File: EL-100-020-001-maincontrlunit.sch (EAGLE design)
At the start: 186 parts, among them T1 WS-TST-90°, U1 VNI4140K-32, U16 24AA256-I/SN, U19 ABS10-32.768KHZ-7-T, U2 VNI4140K-32, U3 VNI4140K-32, U8 MCP7940N-I/SN, U9 PMEG2005ET, X1 944-12-46-00, X10 S2L3.50/8/90G, X11 S2L3.50/8/90G, X12 S2L3.50/8/90G, X13 140-08-FLACHBAND1.27, X14 944-12-2-00, X2 944-12-46-00, X3 90G-14, X4 90G-14, X5 Q-063209, X6 Q-063209, X7 Q-063209, X8 Q-063209, X9 S2L3.50/8/90G

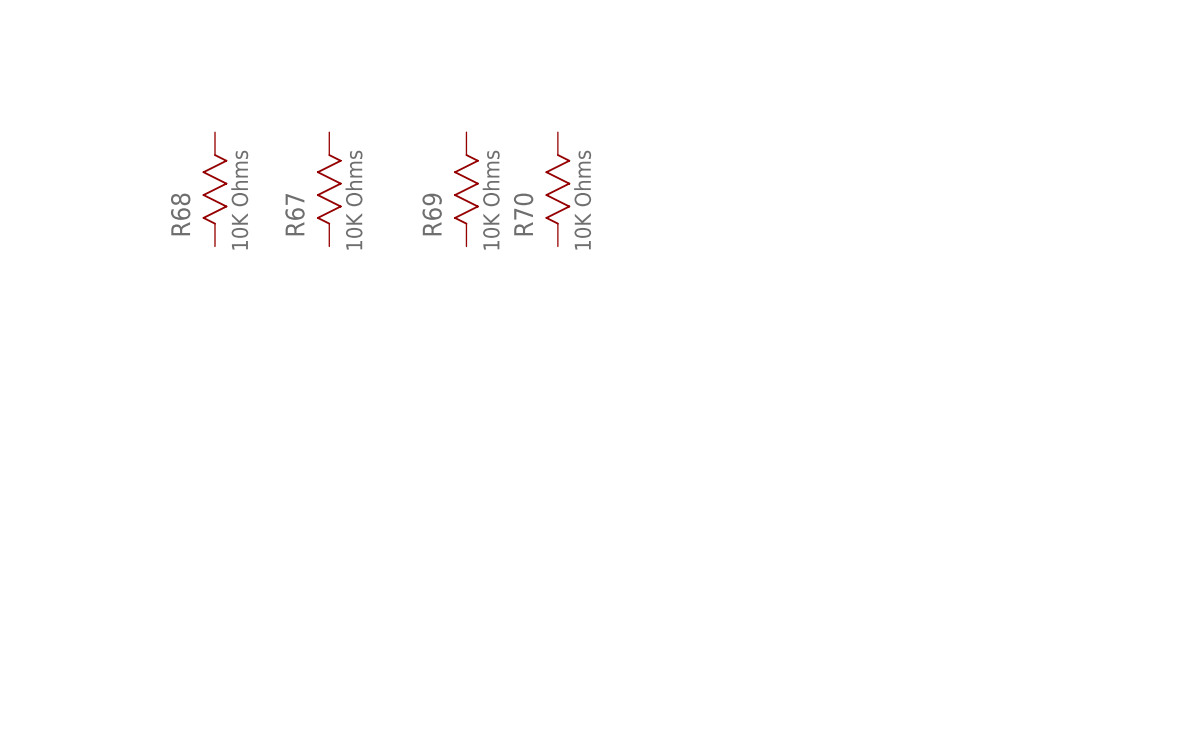
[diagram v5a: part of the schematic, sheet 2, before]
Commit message: update DIN rail
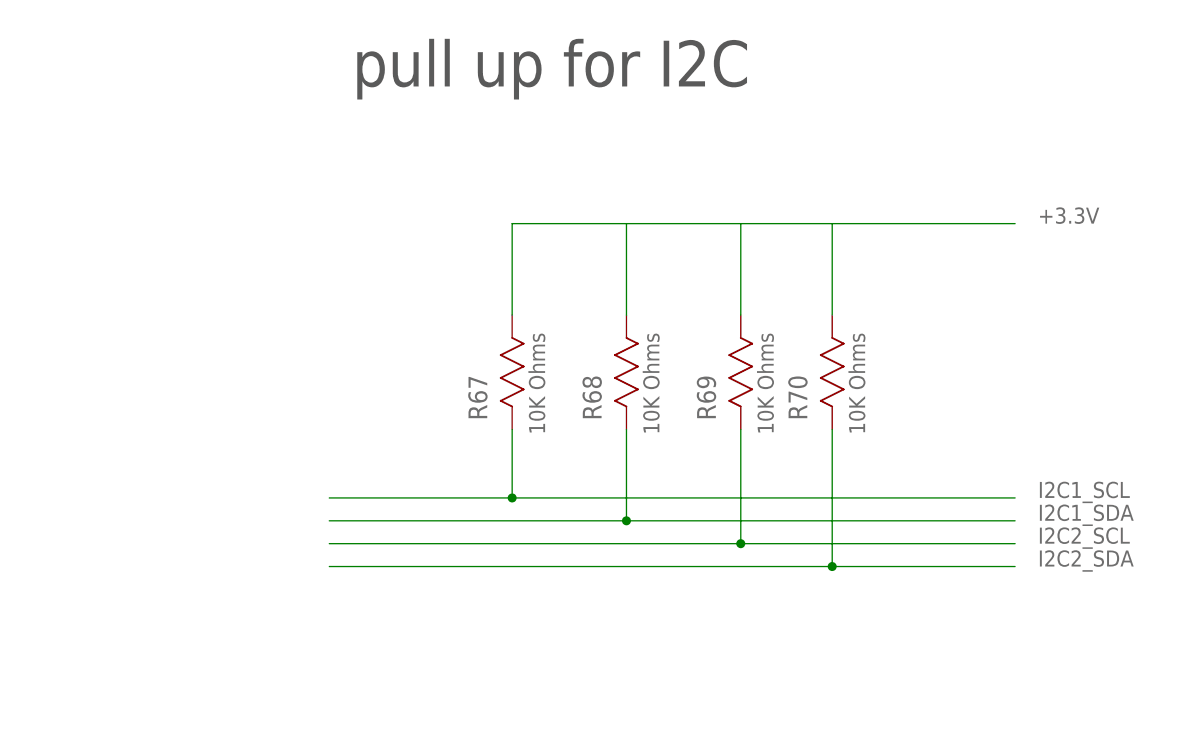
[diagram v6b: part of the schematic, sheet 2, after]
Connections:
- net +3.3V: now also R67.1, R68.1, R69.1, R70.1
- net I2C1_SCL: now also R67.2
- net I2C1_SDA: now also R68.2
- net I2C2_SCL: now also R69.2
- net I2C2_SDA: now also R70.2
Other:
- note added: "pull up for I2C"
- moved on the sheet: R65, R67, R68, R69, R70
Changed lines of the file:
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@@
 <plain>
 <text x="35.56" y="226.06" size="5.08" layer="97" ratio="10">5VDC Filter</text>
+<text x="274.32" y="243.84" size="5.08" layer="97">pull up for I2C</text>
 </plain>
 <instances>
@@
 <instance part="SUPPLY55" gate="G$1" x="55.88" y="200.66"/>
 <instance part="SUPPLY56" gate="G$1" x="68.58" y="200.66"/>
-<instance part="R68" gate="A" x="259.08" y="226.06" smashed="yes" rot="R90">
-<attribute name="VALUE" x="262.7376" y="225.4758" size="1.778" layer="96" rot="SR90"/>
-<attribute name="NAME" x="256.3114" y="227.0506" size="2.0828" layer="95" ratio="10" rot="SR90"/>
-<attribute name="MF" x="259.08" y="226.06" size="1.778" layer="96" display="off"/>
-</instance>
-<instance part="R67" gate="A" x="271.78" y="226.06" smashed="yes" rot="R90">
-<attribute name="VALUE" x="275.4376" y="225.4758" size="1.778" layer="96" rot="SR90"/>
-<attribute name="NAME" x="269.0114" y="227.0506" size="2.0828" layer="95" ratio="10" rot="SR90"/>
-<attribute name="MF" x="271.78" y="226.06" size="1.778" layer="96" display="off"/>
-</instance>
-<instance part="R69" gate="A" x="287.02" y="226.06" smashed="yes" rot="R90">
-<attribute name="VALUE" x="290.6776" y="225.4758" size="1.778" layer="96" rot="SR90"/>
-<attribute name="NAME" x="284.2514" y="227.0506" size="2.0828" layer="95" ratio="10" rot="SR90"/>
-<attribute name="MF" x="287.02" y="226.06" size="1.778" layer="96" display="off"/>
-</instance>
-<instance part="R70" gate="A" x="297.18" y="226.06" smashed="yes" rot="R90">
-<attribute name="VALUE" x="300.8376" y="225.4758" size="1.778" layer="96" rot="SR90"/>
-<attribute name="NAME" x="294.4114" y="227.0506" size="2.0828" layer="95" ratio="10" rot="SR90"/>
-<attribute name="MF" x="297.18" y="226.06" size="1.778" layer="96" display="off"/>
+<instance part="R68" gate="A" x="304.8" y="205.74" smashed="yes" rot="R90">
+<attribute name="VALUE" x="308.4576" y="205.1558" size="1.778" layer="96" rot="SR90"/>
+<attribute name="NAME" x="302.0314" y="206.7306" size="2.0828" layer="95" ratio="10" rot="SR90"/>
+<attribute name="MF" x="304.8" y="205.74" size="1.778" layer="96" display="off"/>
+</instance>
+<instance part="R67" gate="A" x="292.1" y="205.74" smashed="yes" rot="R90">
+<attribute name="VALUE" x="295.7576" y="205.1558" size="1.778" layer="96" rot="SR90"/>
+<attribute name="NAME" x="289.3314" y="206.7306" size="2.0828" layer="95" ratio="10" rot="SR90"/>
+<attribute name="MF" x="292.1" y="205.74" size="1.778" layer="96" display="off"/>
+</instance>
+<instance part="R69" gate="A" x="317.5" y="205.74" smashed="yes" rot="R90">
+<attribute name="VALUE" x="321.1576" y="205.1558" size="1.778" layer="96" rot="SR90"/>
+<attribute name="NAME" x="314.7314" y="206.7306" size="2.0828" layer="95" ratio="10" rot="SR90"/>
+<attribute name="MF" x="317.5" y="205.74" size="1.778" layer="96" display="off"/>
+</instance>
+<instance part="R70" gate="A" x="327.66" y="205.74" smashed="yes" rot="R90">
+<attribute name="VALUE" x="331.3176" y="205.1558" size="1.778" layer="96" rot="SR90"/>
+<attribute name="NAME" x="324.8914" y="206.7306" size="2.0828" layer="95" ratio="10" rot="SR90"/>
+<attribute name="MF" x="327.66" y="205.74" size="1.778" layer="96" display="off"/>
 </instance>
 </instances>
@@
 <pinref part="X1" gate="G$1" pin="4"/>
 </segment>
+<segment>
+<pinref part="R70" gate="A" pin="1"/>
+<wire x1="292.1" y1="228.6" x2="304.8" y2="228.6" width="0.1524" layer="91"/>
+<wire x1="304.8" y1="228.6" x2="317.5" y2="228.6" width="0.1524" layer="91"/>
+<wire x1="317.5" y1="228.6" x2="327.66" y2="228.6" width="0.1524" layer="91"/>
+<wire x1="327.66" y1="228.6" x2="327.66" y2="218.44" width="0.1524" layer="91"/>
+<pinref part="R67" gate="A" pin="1"/>
+<wire x1="292.1" y1="218.44" x2="292.1" y2="228.6" width="0.1524" layer="91"/>
+<pinref part="R68" gate="A" pin="1"/>
+<wire x1="304.8" y1="218.44" x2="304.8" y2="228.6" width="0.1524" layer="91"/>
+<pinref part="R69" gate="A" pin="1"/>
+<wire x1="317.5" y1="218.44" x2="317.5" y2="228.6" width="0.1524" layer="91"/>
+<wire x1="327.66" y1="228.6" x2="347.98" y2="228.6" width="0.1524" layer="91"/>
+<label x="350.52" y="228.6" size="1.778" layer="95"/>
+</segment>
 </net>
 <net name="DGND" class="0">
@@
 <pinref part="X1" gate="G$1" pin="19"/>
 </segment>
+<segment>
+<wire x1="347.98" y1="193.04" x2="317.5" y2="193.04" width="0.1524" layer="91"/>
+<label x="350.52" y="193.04" size="1.778" layer="95"/>
+<pinref part="R69" gate="A" pin="2"/>
+<wire x1="317.5" y1="193.04" x2="271.78" y2="193.04" width="0.1524" layer="91"/>
+<wire x1="317.5" y1="205.74" x2="317.5" y2="193.04" width="0.1524" layer="91"/>
+<junction x="317.5" y="193.04"/>
+</segment>
 </net>
 <net name="I2C2_SDA" class="0">
@@
 <pinref part="X1" gate="G$1" pin="20"/>
 </segment>
+<segment>
+<wire x1="271.78" y1="190.5" x2="327.66" y2="190.5" width="0.1524" layer="91"/>
+<label x="350.52" y="190.5" size="1.778" layer="95"/>
+<pinref part="R70" gate="A" pin="2"/>
+<wire x1="327.66" y1="190.5" x2="347.98" y2="190.5" width="0.1524" layer="91"/>
+<wire x1="327.66" y1="205.74" x2="327.66" y2="190.5" width="0.1524" layer="91"/>
+<junction x="327.66" y="190.5"/>
+</segment>
 </net>
 <net name="P8_19" class="0">
@@
 <pinref part="X1" gate="G$1" pin="18"/>
 </segment>
+<segment>
+<wire x1="271.78" y1="195.58" x2="304.8" y2="195.58" width="0.1524" layer="91"/>
+<label x="350.52" y="195.58" size="1.778" layer="95"/>
+<pinref part="R68" gate="A" pin="2"/>
+<wire x1="304.8" y1="195.58" x2="347.98" y2="195.58" width="0.1524" layer="91"/>
+<wire x1="304.8" y1="205.74" x2="304.8" y2="195.58" width="0.1524" layer="91"/>
+<junction x="304.8" y="195.58"/>
+</segment>
 </net>
 <net name="I2C1_SCL" class="0">
@@
 <pinref part="X1" gate="G$1" pin="17"/>
 </segment>
+<segment>
+<wire x1="347.98" y1="198.12" x2="292.1" y2="198.12" width="0.1524" layer="91"/>
+<label x="350.52" y="198.12" size="1.778" layer="95"/>
+<pinref part="R67" gate="A" pin="2"/>
+<wire x1="292.1" y1="198.12" x2="271.78" y2="198.12" width="0.1524" layer="91"/>
+<wire x1="292.1" y1="205.74" x2="292.1" y2="198.12" width="0.1524" layer="91"/>
+<junction x="292.1" y="198.12"/>
+</segment>
 </net>
 <net name="SYS_RESET" class="0">
@@
 </instance>
 <instance part="SUPPLY106" gate="G$1" x="213.36" y="139.7"/>
-<instance part="R65" gate="A" x="248.92" y="182.88" smashed="yes">
-<attribute name="VALUE" x="250.8758" y="179.2224" size="1.778" layer="96" ratio="10" rot="SR0"/>
-<attribute name="NAME" x="249.9106" y="185.6486" size="2.0828" layer="95" ratio="10" rot="SR0"/>
-<attribute name="MF" x="248.92" y="182.88" size="1.778" layer="96" rot="R270" display="off"/>
+<instance part="R65" gate="A" x="243.84" y="182.88" smashed="yes">
+<attribute name="VALUE" x="245.7958" y="179.2224" size="1.778" layer="96" ratio="10" rot="SR0"/>
+<attribute name="NAME" x="244.8306" y="185.6486" size="2.0828" layer="95" ratio="10" rot="SR0"/>
+<attribute name="MF" x="243.84" y="182.88" size="1.778" layer="96" rot="R270" display="off"/>
 </instance>
 <instance part="X13" gate="G$1" x="66.04" y="180.34" smashed="yes">
@@
 <wire x1="205.74" y1="177.8" x2="213.36" y2="177.8" width="0.1524" layer="91"/>
 <wire x1="213.36" y1="177.8" x2="213.36" y2="162.56" width="0.1524" layer="91"/>
+<junction x="213.36" y="162.56"/>
 </segment>
 <segment>
@@
 <wire x1="205.74" y1="187.96" x2="218.44" y2="187.96" width="0.1524" layer="91"/>
 <wire x1="218.44" y1="187.96" x2="218.44" y2="182.88" width="0.1524" layer="91"/>
-<wire x1="218.44" y1="182.88" x2="248.92" y2="182.88" width="0.1524" layer="91"/>
+<wire x1="218.44" y1="182.88" x2="243.84" y2="182.88" width="0.1524" layer="91"/>
 <pinref part="R65" gate="A" pin="2"/>
 </segment>
@@
 <segment>
 <pinref part="R65" gate="A" pin="1"/>
-<wire x1="261.62" y1="182.88" x2="271.78" y2="182.88" width="0.1524" layer="91"/>
+<wire x1="256.54" y1="182.88" x2="271.78" y2="182.88" width="0.1524" layer="91"/>
 <label x="274.32" y="182.88" size="1.778" layer="95"/>
 </segment>

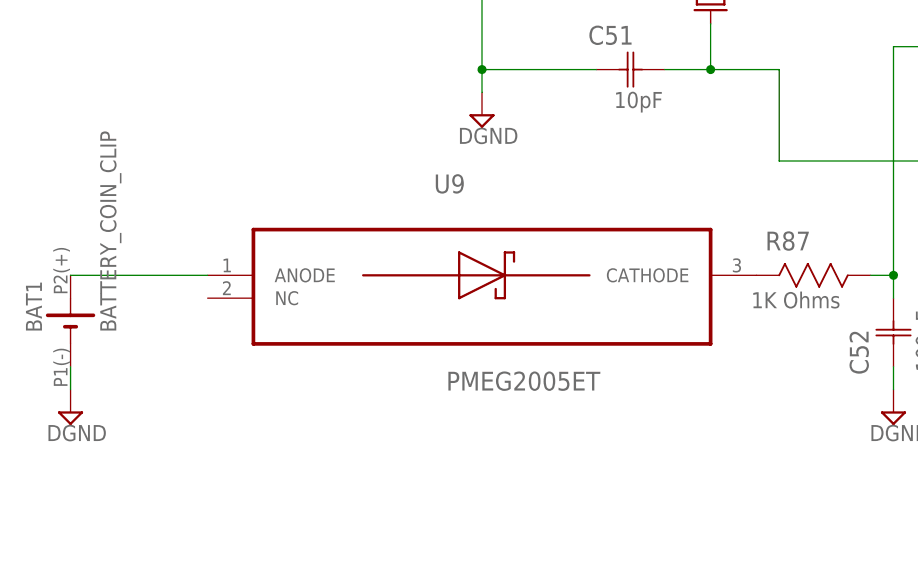
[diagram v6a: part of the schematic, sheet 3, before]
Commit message: update DIN rail
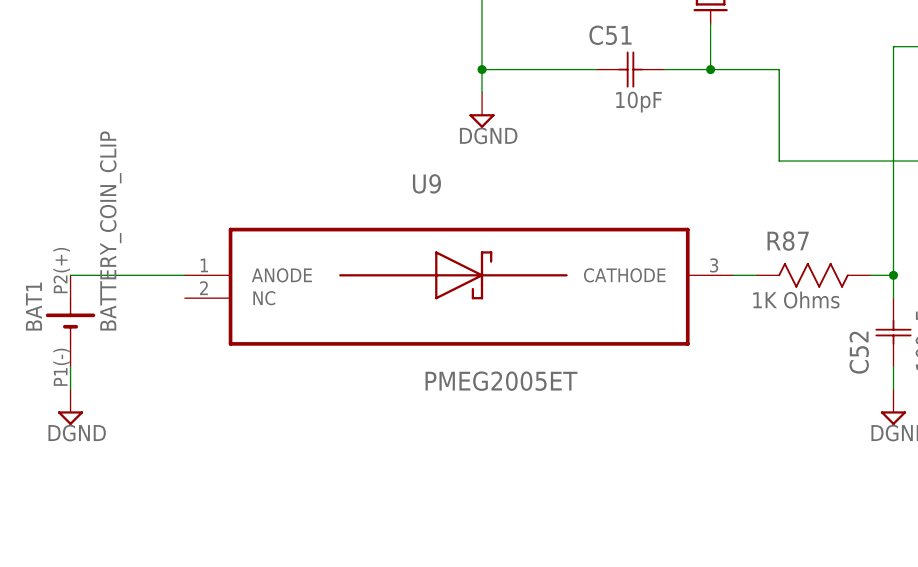
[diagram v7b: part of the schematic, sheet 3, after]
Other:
- moved on the sheet: U9
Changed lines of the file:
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@@
 <attribute name="MF" x="185.42" y="185.42" size="1.778" layer="96" display="off"/>
 </instance>
-<instance part="U9" gate="A" x="111.76" y="167.64">
-<attribute name="MF" x="111.76" y="167.64" size="1.778" layer="96" display="off"/>
+<instance part="U9" gate="A" x="109.22" y="167.64">
+<attribute name="MF" x="109.22" y="167.64" size="1.778" layer="96" display="off"/>
 </instance>
 <instance part="U19" gate="G$1" x="137.16" y="195.58" rot="R90">
@@
 <pinref part="BAT1" gate="G$1" pin="+"/>
 <pinref part="U9" gate="A" pin="ANODE"/>
-<wire x1="66.04" y1="165.1" x2="81.28" y2="165.1" width="0.1524" layer="91"/>
+<wire x1="66.04" y1="165.1" x2="78.74" y2="165.1" width="0.1524" layer="91"/>
 </segment>
 </net>
@@
 <pinref part="U9" gate="A" pin="CATHODE"/>
 <pinref part="R87" gate="A" pin="2"/>
+<wire x1="139.7" y1="165.1" x2="142.24" y2="165.1" width="0.1524" layer="91"/>
 </segment>
 </net>
@@
 <instance part="R62" gate="A" x="238.76" y="190.5" smashed="yes" rot="R90">
 <attribute name="VALUE" x="242.4176" y="192.4558" size="1.778" layer="96" ratio="10" rot="SR90"/>
-<attribute name="NAME" x="235.9914" y="191.4906" size="2.0828" layer="95" ratio="10" rot="SR90"/>
+<attribute name="NAME" x="235.9914" y="194.0306" size="2.0828" layer="95" ratio="10" rot="SR90"/>
 <attribute name="MF" x="238.76" y="190.5" size="1.778" layer="96" display="off"/>
 </instance>

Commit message: Din rail
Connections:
- net VADC_1.8V: now also X5.B10
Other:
- moved on the sheet: R65
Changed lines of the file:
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@@
 <label x="350.52" y="193.04" size="1.778" layer="95"/>
 <pinref part="R69" gate="A" pin="2"/>
-<wire x1="317.5" y1="193.04" x2="271.78" y2="193.04" width="0.1524" layer="91"/>
+<wire x1="317.5" y1="193.04" x2="254" y2="193.04" width="0.1524" layer="91"/>
 <wire x1="317.5" y1="205.74" x2="317.5" y2="193.04" width="0.1524" layer="91"/>
 <junction x="317.5" y="193.04"/>
@@
 </segment>
 <segment>
-<wire x1="271.78" y1="190.5" x2="327.66" y2="190.5" width="0.1524" layer="91"/>
 <label x="350.52" y="190.5" size="1.778" layer="95"/>
 <pinref part="R70" gate="A" pin="2"/>
+<wire x1="246.38" y1="190.5" x2="327.66" y2="190.5" width="0.1524" layer="91"/>
 <wire x1="327.66" y1="190.5" x2="347.98" y2="190.5" width="0.1524" layer="91"/>
 <wire x1="327.66" y1="205.74" x2="327.66" y2="190.5" width="0.1524" layer="91"/>
@@
 </segment>
 <segment>
-<wire x1="271.78" y1="195.58" x2="304.8" y2="195.58" width="0.1524" layer="91"/>
 <label x="350.52" y="195.58" size="1.778" layer="95"/>
 <pinref part="R68" gate="A" pin="2"/>
+<wire x1="264.16" y1="195.58" x2="304.8" y2="195.58" width="0.1524" layer="91"/>
 <wire x1="304.8" y1="195.58" x2="347.98" y2="195.58" width="0.1524" layer="91"/>
 <wire x1="304.8" y1="205.74" x2="304.8" y2="195.58" width="0.1524" layer="91"/>
@@
 </segment>
 </net>
+<net name="VADC_1.8V" class="0">
+<segment>
+<pinref part="X5" gate="G$1" pin="B10"/>
+<wire x1="157.48" y1="180.34" x2="165.1" y2="180.34" width="0.1524" layer="91"/>
+<label x="165.1" y="180.34" size="1.778" layer="95"/>
+</segment>
+</net>
 </nets>
 </sheet>
@@
 </instance>
 <instance part="SUPPLY106" gate="G$1" x="213.36" y="139.7"/>
-<instance part="R65" gate="A" x="243.84" y="182.88" smashed="yes">
-<attribute name="VALUE" x="245.7958" y="179.2224" size="1.778" layer="96" ratio="10" rot="SR0"/>
-<attribute name="NAME" x="244.8306" y="185.6486" size="2.0828" layer="95" ratio="10" rot="SR0"/>
-<attribute name="MF" x="243.84" y="182.88" size="1.778" layer="96" rot="R270" display="off"/>
+<instance part="R65" gate="A" x="251.46" y="182.88" smashed="yes">
+<attribute name="VALUE" x="253.4158" y="179.2224" size="1.778" layer="96" ratio="10" rot="SR0"/>
+<attribute name="NAME" x="252.4506" y="185.6486" size="2.0828" layer="95" ratio="10" rot="SR0"/>
+<attribute name="MF" x="251.46" y="182.88" size="1.778" layer="96" rot="R270" display="off"/>
 </instance>
 <instance part="X13" gate="G$1" x="66.04" y="180.34" smashed="yes">
@@
 <wire x1="205.74" y1="187.96" x2="218.44" y2="187.96" width="0.1524" layer="91"/>
 <wire x1="218.44" y1="187.96" x2="218.44" y2="182.88" width="0.1524" layer="91"/>
-<wire x1="218.44" y1="182.88" x2="243.84" y2="182.88" width="0.1524" layer="91"/>
+<wire x1="218.44" y1="182.88" x2="251.46" y2="182.88" width="0.1524" layer="91"/>
 <pinref part="R65" gate="A" pin="2"/>
 </segment>
@@
 <segment>
 <pinref part="R65" gate="A" pin="1"/>
-<wire x1="256.54" y1="182.88" x2="271.78" y2="182.88" width="0.1524" layer="91"/>
+<wire x1="264.16" y1="182.88" x2="271.78" y2="182.88" width="0.1524" layer="91"/>
 <label x="274.32" y="182.88" size="1.778" layer="95"/>
 </segment>
